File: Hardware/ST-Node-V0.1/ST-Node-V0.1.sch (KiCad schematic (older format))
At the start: 0 parts

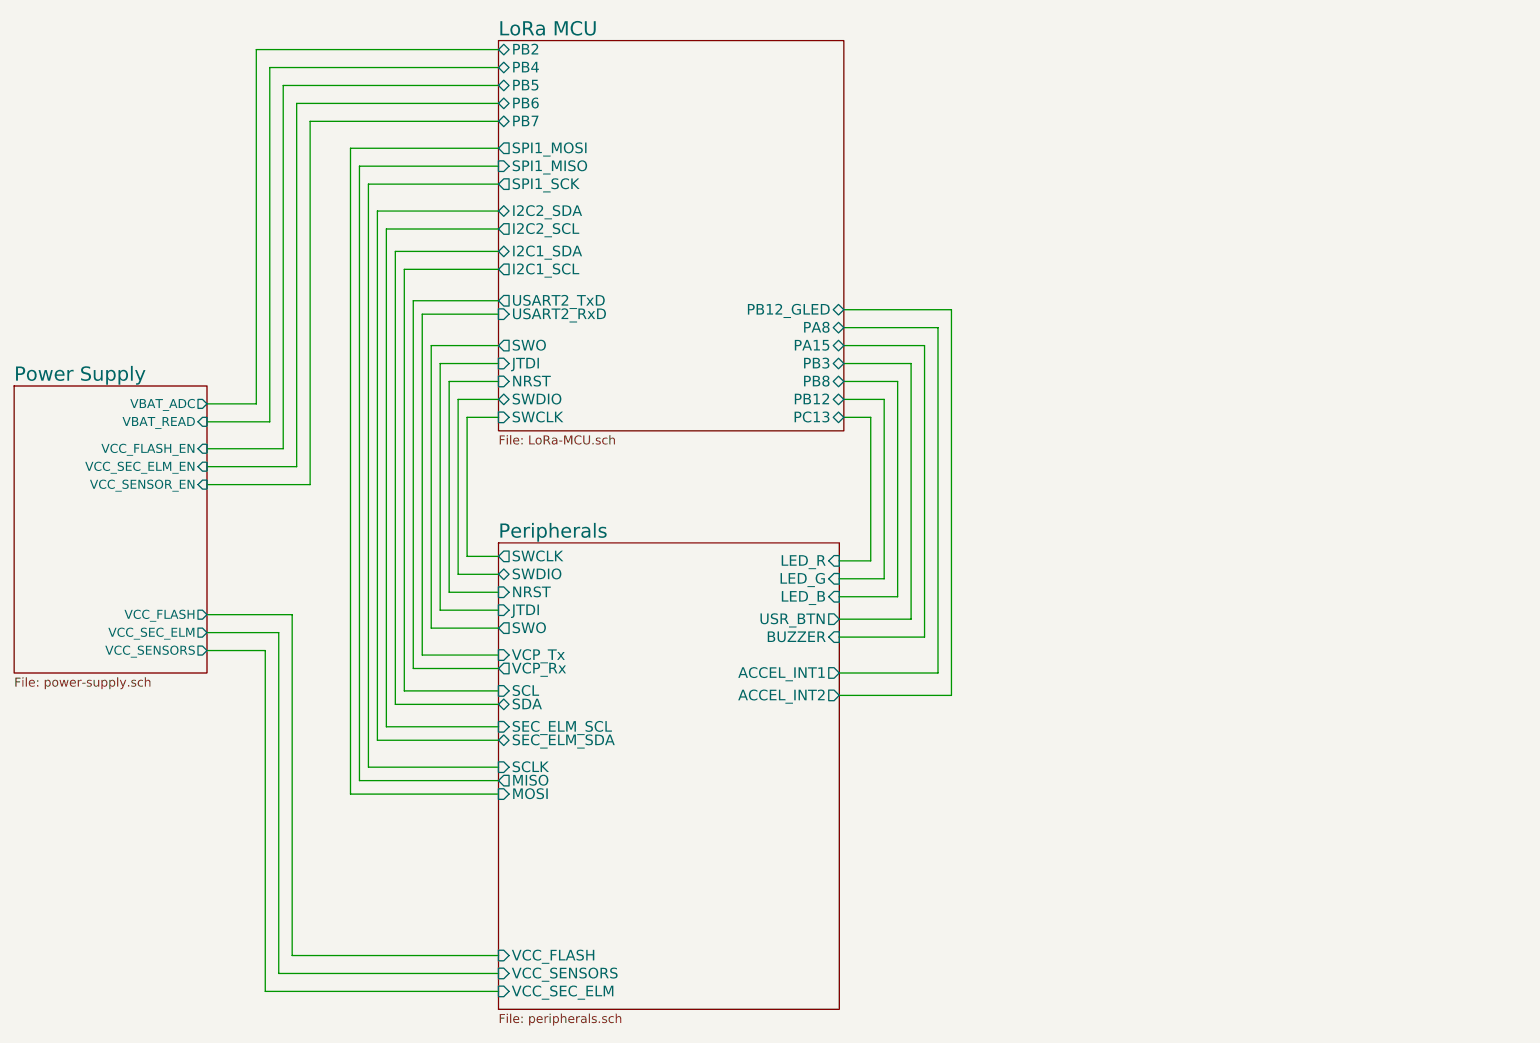
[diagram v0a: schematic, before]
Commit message: sch:  Swap couple of pins and fix a HW bug
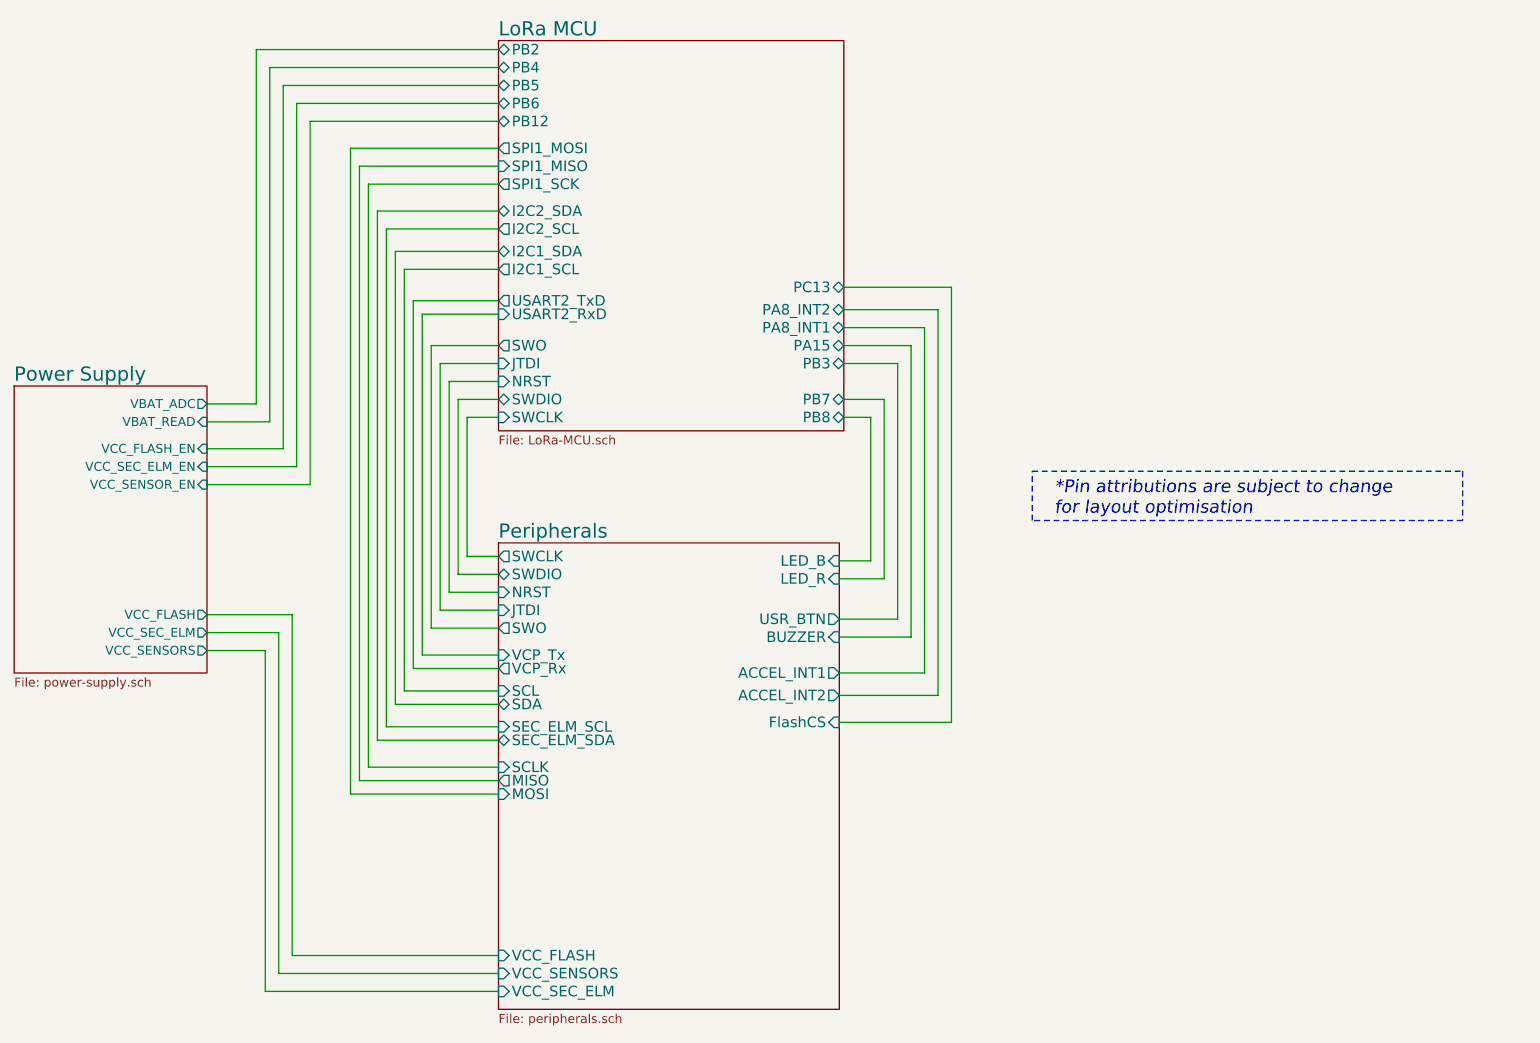
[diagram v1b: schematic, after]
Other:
- note added: "*Pin attributions are subject to change \nfor layout optimisation"
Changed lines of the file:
@@
 F13 "SEC_ELM_SDA" B L 5575 4650 59
 F14 "BUZZER" I R 7475 4075 59
-F15 "LED_R" I R 7475 3650 59
-F16 "LED_G" I R 7475 3750 59
-F17 "LED_B" I R 7475 3850 59
-F18 "USR_BTN" O R 7475 3975 59
-F19 "NRST" I L 5575 3825 59
-F20 "JTDI" I L 5575 3925 59
-F21 "SWO" O L 5575 4025 59
-F22 "SWCLK" O L 5575 3625 59
-F23 "SWDIO" B L 5575 3725 59
-F24 "VCP_Rx" O L 5575 4250 59
-F25 "VCP_Tx" I L 5575 4175 59
+F15 "LED_R" I R 7475 3750 59
+F16 "LED_B" I R 7475 3650 59
+F17 "USR_BTN" O R 7475 3975 59
+F18 "NRST" I L 5575 3825 59
+F19 "JTDI" I L 5575 3925 59
+F20 "SWO" O L 5575 4025 59
+F21 "SWCLK" O L 5575 3625 59
+F22 "SWDIO" B L 5575 3725 59
+F23 "VCP_Rx" O L 5575 4250 59
+F24 "VCP_Tx" I L 5575 4175 59
+F25 "FlashCS" I R 7475 4550 59
 $EndSheet
 $Bitmap
@@
 F7 "USART2_TxD" O L 5575 2200 59
 F8 "USART2_RxD" I L 5575 2275 59
-F9 "PB8" B R 7500 2650 59
-F10 "PB12" B R 7500 2750 59
-F11 "PC13" B R 7500 2850 59
+F9 "PB8" B R 7500 2850 59
+F10 "PB12" B L 5575 1200 59
+F11 "PC13" B R 7500 2125 59
 F12 "I2C2_SDA" B L 5575 1700 59
 F13 "I2C2_SCL" O L 5575 1800 59
@@
 F17 "SPI1_MISO" I L 5575 1450 59
 F18 "SPI1_MOSI" O L 5575 1350 59
-F19 "PB7" B L 5575 1200 59
+F19 "PB7" B R 7500 2750 59
 F20 "PB6" B L 5575 1100 59
 F21 "PB5" B L 5575 1000 59
 F22 "PB4" B L 5575 900 59
 F23 "PB2" B L 5575 800 59
-F24 "PA8" B R 7500 2350 59
-F25 "PB3" B R 7500 2550 59
-F26 "PA15" B R 7500 2450 59
-F27 "PB12_GLED" B R 7500 2250 59
+F24 "PB3" B R 7500 2550 59
+F25 "PA15" B R 7500 2450 59
+F26 "PA8_INT2" B R 7500 2250 59
+F27 "PA8_INT1" B R 7500 2350 59
 $EndSheet
 Wire Wire Line
@@
 	7725 3750 7475 3750
 Wire Wire Line
-	7500 2650 7800 2650
-Wire Wire Line
-	7800 2650 7800 3850
-Wire Wire Line
-	7800 3850 7475 3850
-Wire Wire Line
 	3950 3950 4425 3950
 Wire Wire Line
@@
 	4525 1200 5575 1200
 Wire Wire Line
-	7500 2550 7875 2550
+	7500 2550 7800 2550
+Wire Wire Line
+	7800 2550 7800 3975
+Wire Wire Line
+	7800 3975 7475 3975
+Wire Wire Line
+	7500 2450 7875 2450
 Wire Wire Line
-	7875 2550 7875 3975
+	7875 2450 7875 4075
 Wire Wire Line
-	7875 3975 7475 3975
+	7875 4075 7475 4075
 Wire Wire Line
-	7500 2450 7950 2450
+	7500 2350 7950 2350
 Wire Wire Line
-	7950 2450 7950 4075
+	7950 2350 7950 4275
 Wire Wire Line
-	7950 4075 7475 4075
+	7950 4275 7475 4275
 Wire Wire Line
-	7500 2350 8025 2350
+	7500 2250 8025 2250
 Wire Wire Line
-	8025 2350 8025 4275
+	8025 2250 8025 4400
 Wire Wire Line
-	8025 4275 7475 4275
+	8025 4400 7475 4400
 Wire Wire Line
-	7500 2250 8100 2250
+	7500 2125 8100 2125
 Wire Wire Line
-	8100 2250 8100 4400
+	8100 2125 8100 4550
 Wire Wire Line
-	8100 4400 7475 4400
+	8100 4550 7475 4550
+Text Notes 8675 3400 0    71   Italic 0
+*Pin attributions are subject to change \nfor layout optimisation
+Wire Notes Line
+	10950 3150 10950 3425
+Wire Notes Line
+	10950 3425 8550 3425
+Wire Notes Line
+	8550 3425 8550 3150
+Wire Notes Line
+	8550 3150 10950 3150
 $EndSCHEMATC
